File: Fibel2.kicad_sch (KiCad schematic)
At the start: 0 parts

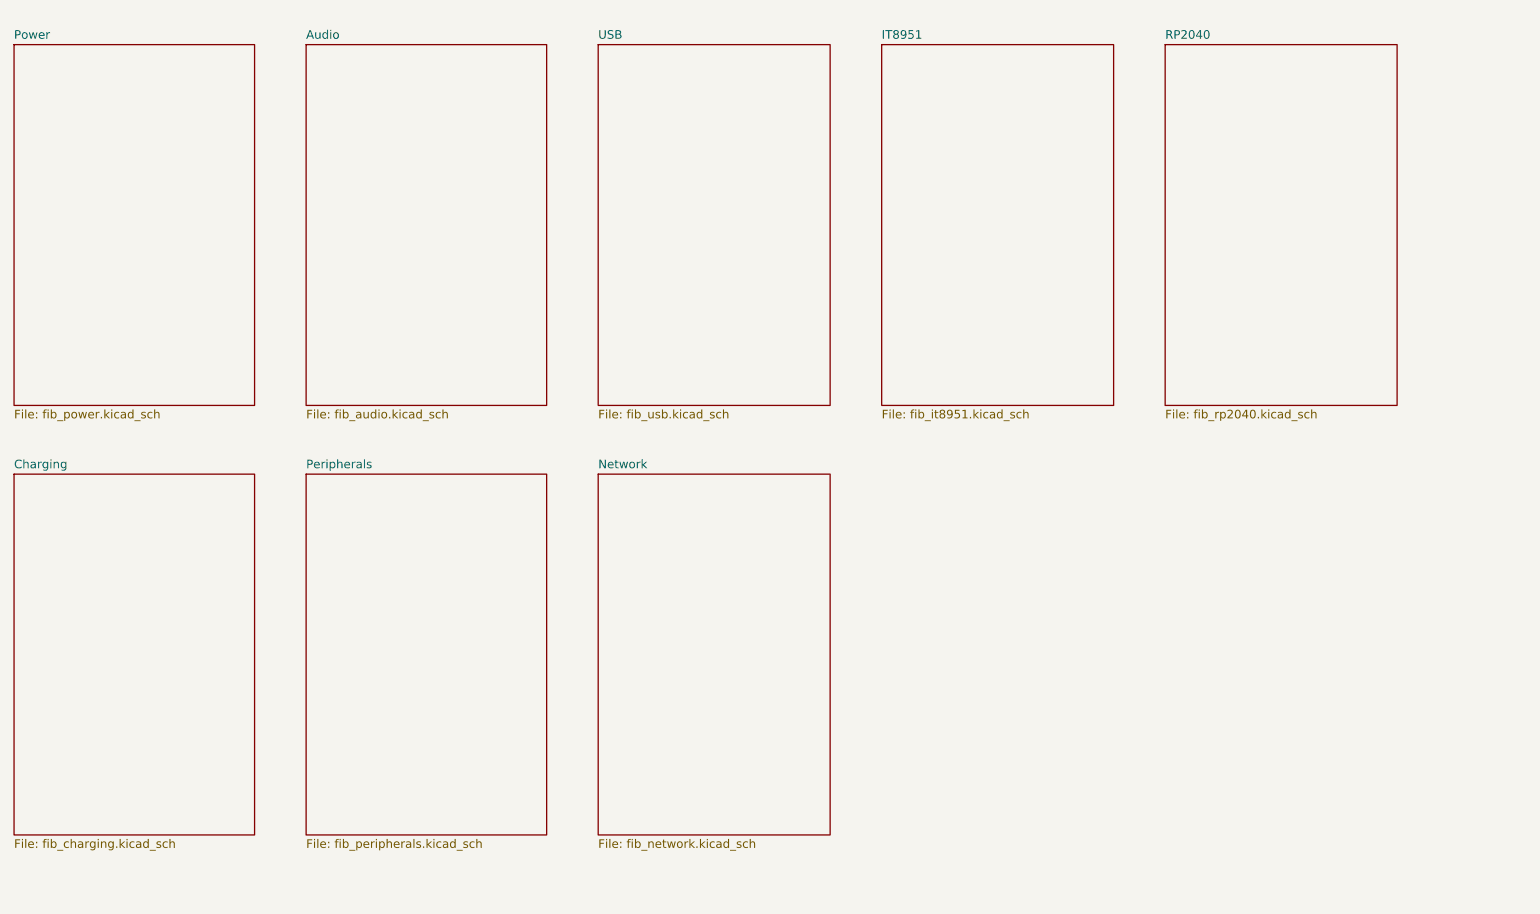
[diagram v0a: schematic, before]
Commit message: added several ICs, implementted schematics for charger, boost converter and LDOs
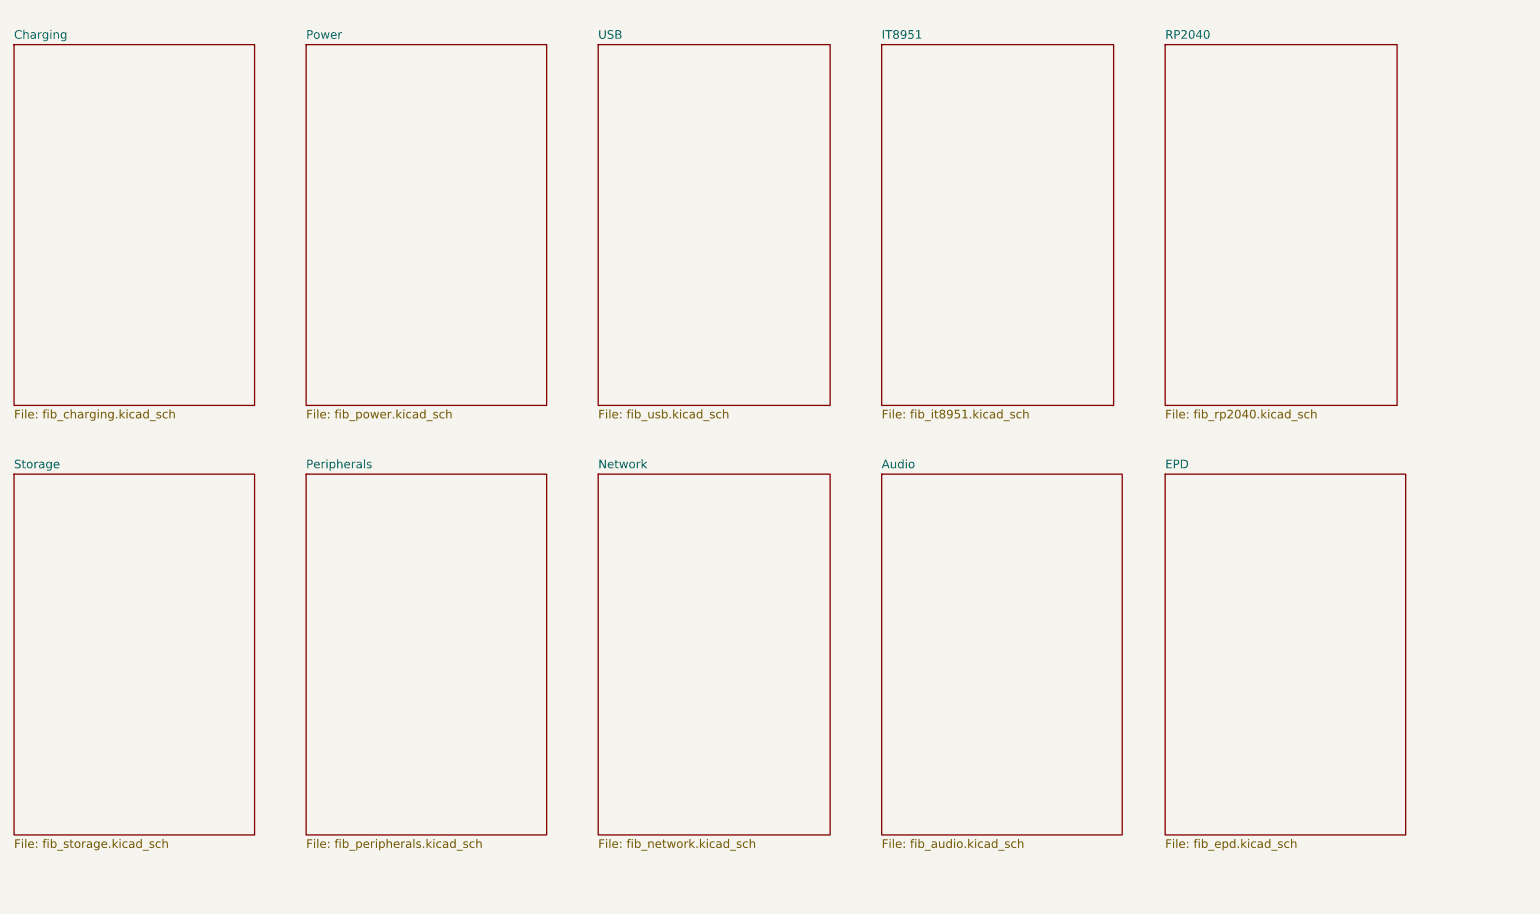
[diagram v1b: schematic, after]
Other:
- added sheet EPD (fib_epd.kicad_sch)
- added sheet Storage (fib_storage.kicad_sch)
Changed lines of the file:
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@@
 	(paper "A4")
 	(sheet
-		(at 69.85 21.59)
+		(at 154.94 85.09)
 		(size 35.56 53.34)
 		(fields_autoplaced yes)
@@
 		)
 		(property "Sheetname" "Audio"
-			(at 69.85 20.8784 0)
+			(at 154.94 84.3784 0)
 			(effects
 				(font
@@
 		)
 		(property "Sheetfile" "fib_audio.kicad_sch"
-			(at 69.85 75.5146 0)
+			(at 154.94 139.0146 0)
 			(effects
 				(font
@@
 	)
 	(sheet
-		(at 26.67 85.09)
+		(at 26.67 21.59)
 		(size 35.56 53.34)
 		(fields_autoplaced yes)
@@
 		)
 		(property "Sheetname" "Charging"
-			(at 26.67 84.3784 0)
+			(at 26.67 20.8784 0)
 			(effects
 				(font
@@
 		)
 		(property "Sheetfile" "fib_charging.kicad_sch"
-			(at 26.67 139.0146 0)
+			(at 26.67 75.5146 0)
 			(effects
 				(font
@@
 	)
 	(sheet
-		(at 26.67 21.59)
+		(at 196.85 85.09)
+		(size 35.56 53.34)
+		(fields_autoplaced yes)
+		(stroke
+			(width 0.1524)
+			(type solid)
+		)
+		(fill
+			(color 0 0 0 0.0000)
+		)
+		(property "Sheetname" "EPD"
+			(at 196.85 84.3784 0)
+			(effects
+				(font
+					(size 1.27 1.27)
+				)
+				(justify left bottom)
+			)
+		)
+		(property "Sheetfile" "fib_epd.kicad_sch"
+			(at 196.85 139.0146 0)
+			(effects
+				(font
+					(size 1.27 1.27)
+				)
+				(justify left top)
+			)
+		)
+		(instances
+			(project "Fibel2"
+				(path "/862c21e2-7ec9-4f80-a33c-aad02ea9423e"
+					(page "11")
+				)
+			)
+		)
+	)
+	(sheet
+		(at 26.67 85.09)
+		(size 35.56 53.34)
+		(fields_autoplaced yes)
+		(stroke
+			(width 0.1524)
+			(type solid)
+		)
+		(fill
+			(color 0 0 0 0.0000)
+		)
+		(property "Sheetname" "Storage"
+			(at 26.67 84.3784 0)
+			(effects
+				(font
+					(size 1.27 1.27)
+				)
+				(justify left bottom)
+			)
+		)
+		(property "Sheetfile" "fib_storage.kicad_sch"
+			(at 26.67 139.0146 0)
+			(effects
+				(font
+					(size 1.27 1.27)
+				)
+				(justify left top)
+			)
+		)
+		(instances
+			(project "Fibel2"
+				(path "/862c21e2-7ec9-4f80-a33c-aad02ea9423e"
+					(page "10")
+				)
+			)
+		)
+	)
+	(sheet
+		(at 69.85 21.59)
 		(size 35.56 53.34)
 		(fields_autoplaced yes)
@@
 		)
 		(property "Sheetname" "Power"
-			(at 26.67 20.8784 0)
+			(at 69.85 20.8784 0)
 			(effects
 				(font
@@
 		)
 		(property "Sheetfile" "fib_power.kicad_sch"
-			(at 26.67 75.5146 0)
-			(effects
-				(font
+			(at 69.85 75.5146 0)
+			(effects
+				(font

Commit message: added symbol&footprint for orin/sodimm, added a bunch of specs and docs, partially implemented audio, full steam ahead
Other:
- added sheet Orin_1 (fib_orin_1.kicad_sch)
- added sheet Orin_2 (fib_orin_2.kicad_sch)
- added sheet Orin_3 (fib_orin_3.kicad_sch)
- added sheet Orin_4 (fib_orin_4.kicad_sch)
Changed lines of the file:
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@@
 	(paper "A4")
 	(sheet
-		(at 154.94 85.09)
-		(size 35.56 53.34)
+		(at 154.94 63.5)
+		(size 35.56 38.1)
 		(fields_autoplaced yes)
 		(stroke
@@
 		)
 		(property "Sheetname" "Audio"
-			(at 154.94 84.3784 0)
+			(at 154.94 62.7884 0)
 			(effects
 				(font
@@
 		)
 		(property "Sheetfile" "fib_audio.kicad_sch"
-			(at 154.94 139.0146 0)
+			(at 154.94 101.5496 0)
 			(effects
 				(font
@@
 	)
 	(sheet
-		(at 26.67 21.59)
-		(size 35.56 53.34)
+		(at 26.67 20.32)
+		(size 35.56 38.1)
 		(fields_autoplaced yes)
 		(stroke
@@
 		)
 		(property "Sheetname" "Charging"
-			(at 26.67 20.8784 0)
+			(at 26.67 19.6084 0)
 			(effects
 				(font
@@
 		)
 		(property "Sheetfile" "fib_charging.kicad_sch"
-			(at 26.67 75.5146 0)
+			(at 26.67 58.3696 0)
 			(effects
 				(font
@@
 	)
 	(sheet
-		(at 196.85 21.59)
-		(size 34.29 53.34)
+		(at 196.85 20.32)
+		(size 34.29 38.1)
 		(fields_autoplaced yes)
 		(stroke
@@
 		)
 		(property "Sheetname" "RP2040"
-			(at 196.85 20.8784 0)
+			(at 196.85 19.05 0)
 			(effects
 				(font
@@
 		)
 		(property "Sheetfile" "fib_rp2040.kicad_sch"
-			(at 196.85 75.5146 0)
+			(at 196.85 58.3696 0)
 			(effects
 				(font
@@
 	)
 	(sheet
-		(at 196.85 85.09)
-		(size 35.56 53.34)
+		(at 113.03 106.68)
+		(size 35.56 38.1)
+		(fields_autoplaced yes)
+		(stroke
+			(width 0.1524)
+			(type solid)
+		)
+		(fill
+			(color 0 0 0 0.0000)
+		)
+		(property "Sheetname" "Orin_3"
+			(at 113.03 105.9684 0)
+			(effects
+				(font
+					(size 1.27 1.27)
+				)
+				(justify left bottom)
+			)
+		)
+		(property "Sheetfile" "fib_orin_3.kicad_sch"
+			(at 113.03 144.7296 0)
+			(effects
+				(font
+					(size 1.27 1.27)
+				)
+				(justify left top)
+			)
+		)
+		(instances
+			(project "Fibel2"
+				(path "/862c21e2-7ec9-4f80-a33c-aad02ea9423e"
+					(page "14")
+				)
+			)
+		)
+	)
+	(sheet
+		(at 196.85 63.5)
+		(size 35.56 38.1)
 		(fields_autoplaced yes)
 		(stroke
@@
 		)
 		(property "Sheetname" "EPD"
-			(at 196.85 84.3784 0)
+			(at 196.85 62.7884 0)
 			(effects
 				(font
@@
 		)
 		(property "Sheetfile" "fib_epd.kicad_sch"
-			(at 196.85 139.0146 0)
+			(at 196.85 101.5496 0)
 			(effects
 				(font
@@
 	)
 	(sheet
-		(at 26.67 85.09)
-		(size 35.56 53.34)
+		(at 69.85 106.68)
+		(size 35.56 38.1)
+		(fields_autoplaced yes)
+		(stroke
+			(width 0.1524)
+			(type solid)
+		)
+		(fill
+			(color 0 0 0 0.0000)
+		)
+		(property "Sheetname" "Orin_2"
+			(at 69.85 105.9684 0)
+			(effects
+				(font
+					(size 1.27 1.27)
+				)
+				(justify left bottom)
+			)
+		)
+		(property "Sheetfile" "fib_orin_2.kicad_sch"
+			(at 69.85 144.7296 0)
+			(effects
+				(font
+					(size 1.27 1.27)
+				)
+				(justify left top)
+			)
+		)
+		(instances
+			(project "Fibel2"
+				(path "/862c21e2-7ec9-4f80-a33c-aad02ea9423e"
+					(page "13")
+				)
+			)
+		)
+	)
+	(sheet
+		(at 26.67 63.5)
+		(size 35.56 38.1)
 		(fields_autoplaced yes)
 		(stroke
@@
 		)
 		(property "Sheetname" "Storage"
-			(at 26.67 84.3784 0)
+			(at 26.67 62.7884 0)
 			(effects
 				(font
@@
 		)
 		(property "Sheetfile" "fib_storage.kicad_sch"
-			(at 26.67 139.0146 0)
+			(at 26.67 101.5496 0)
 			(effects
 				(font
@@
 	)
 	(sheet
-		(at 69.85 21.59)
-		(size 35.56 53.34)
+		(at 69.85 20.32)
+		(size 35.56 38.1)
 		(fields_autoplaced yes)
 		(stroke
@@
 		)
 		(property "Sheetname" "Power"
-			(at 69.85 20.8784 0)
+			(at 69.85 19.6084 0)
 			(effects
 				(font
@@
 		)
 		(property "Sheetfile" "fib_power.kicad_sch"
-			(at 69.85 75.5146 0)
+			(at 69.85 58.3696 0)
 			(effects
 				(font
@@
 	)
 	(sheet
-		(at 113.03 21.59)
-		(size 34.29 53.34)
+		(at 113.03 20.32)
+		(size 34.29 38.1)
 		(fields_autoplaced yes)
 		(stroke
@@
 		)
 		(property "Sheetname" "USB"
-			(at 113.03 20.8784 0)
+			(at 113.03 19.6084 0)
 			(effects
 				(font
@@
 		)
 		(property "Sheetfile" "fib_usb.kicad_sch"
-			(at 113.03 75.5146 0)
+			(at 113.03 58.3696 0)
 			(effects
 				(font
@@
 	)
 	(sheet
-		(at 69.85 85.09)
-		(size 35.56 53.34)
+		(at 69.85 63.5)
+		(size 35.56 38.1)
 		(fields_autoplaced yes)
 		(stroke
@@
 		)
 		(property "Sheetname" "Peripherals"
-			(at 69.85 84.3784 0)
+			(at 69.85 62.7884 0)
 			(effects
 				(font
@@
 		)
 		(property "Sheetfile" "fib_peripherals.kicad_sch"
-			(at 69.85 139.0146 0)
+			(at 69.85 101.5496 0)
 			(effects
 				(font
@@
 	)
 	(sheet
-		(at 113.03 85.09)
-		(size 34.29 53.34)
+		(at 113.03 63.5)
+		(size 34.29 38.1)
 		(fields_autoplaced yes)
 		(stroke
@@
 		)
 		(property "Sheetname" "Network"
-			(at 113.03 84.3784 0)
+			(at 113.03 62.7884 0)
 			(effects
 				(font
@@
 		)
 		(property "Sheetfile" "fib_network.kicad_sch"
-			(at 113.03 139.0146 0)
+			(at 113.03 101.5496 0)
 			(effects
 				(font
@@
 	)
 	(sheet
-		(at 154.94 21.59)
-		(size 34.29 53.34)
+		(at 26.67 106.68)
+		(size 35.56 38.1)
+		(fields_autoplaced yes)
+		(stroke
+			(width 0.1524)
+			(type solid)
+		)
+		(fill
+			(color 0 0 0 0.0000)
+		)
+		(property "Sheetname" "Orin_1"
+			(at 26.67 105.9684 0)
+			(effects
+				(font
+					(size 1.27 1.27)
+				)
+				(justify left bottom)
+			)
+		)
+		(property "Sheetfile" "fib_orin_1.kicad_sch"
+			(at 26.67 144.7296 0)
+			(effects
+				(font
+					(size 1.27 1.27)
+				)
+				(justify left top)
+			)
+		)
+		(instances
+			(project "Fibel2"
+				(path "/862c21e2-7ec9-4f80-a33c-aad02ea9423e"
+					(page "12")
+				)
+			)
+		)
+	)
+	(sheet
+		(at 154.94 106.68)
+		(size 35.56 38.1)
+		(fields_autoplaced yes)
+		(stroke
+			(width 0.1524)
+			(type solid)
+		)
+		(fill
+			(color 0 0 0 0.0000)
+		)
+		(property "Sheetname" "Orin_4"
+			(at 154.94 105.9684 0)
+			(effects
+				(font
+					(size 1.27 1.27)
+				)
+				(justify left bottom)
+			)
+		)
+		(property "Sheetfile" "fib_orin_4.kicad_sch"
+			(at 154.94 144.7296 0)
+			(effects
+				(font
+					(size 1.27 1.27)
+				)
+				(justify left top)
+			)
+		)
+		(instances
+			(project "Fibel2"
+				(path "/862c21e2-7ec9-4f80-a33c-aad02ea9423e"
+					(page "15")
+				)
+			)
+		)
+	)
+	(sheet
+		(at 154.94 20.32)
+		(size 34.29 38.1)
 		(fields_autoplaced yes)
 		(stroke
@@
 		)
 		(property "Sheetname" "IT8951"
-			(at 154.94 20.8784 0)
+			(at 154.94 19.6084 0)
 			(effects
 				(font
@@
 		)
 		(property "Sheetfile" "fib_it8951.kicad_sch"
-			(at 154.94 75.5146 0)
-			(effects
-				(font
+			(at 154.94 58.3696 0)
+			(effects
+				(font

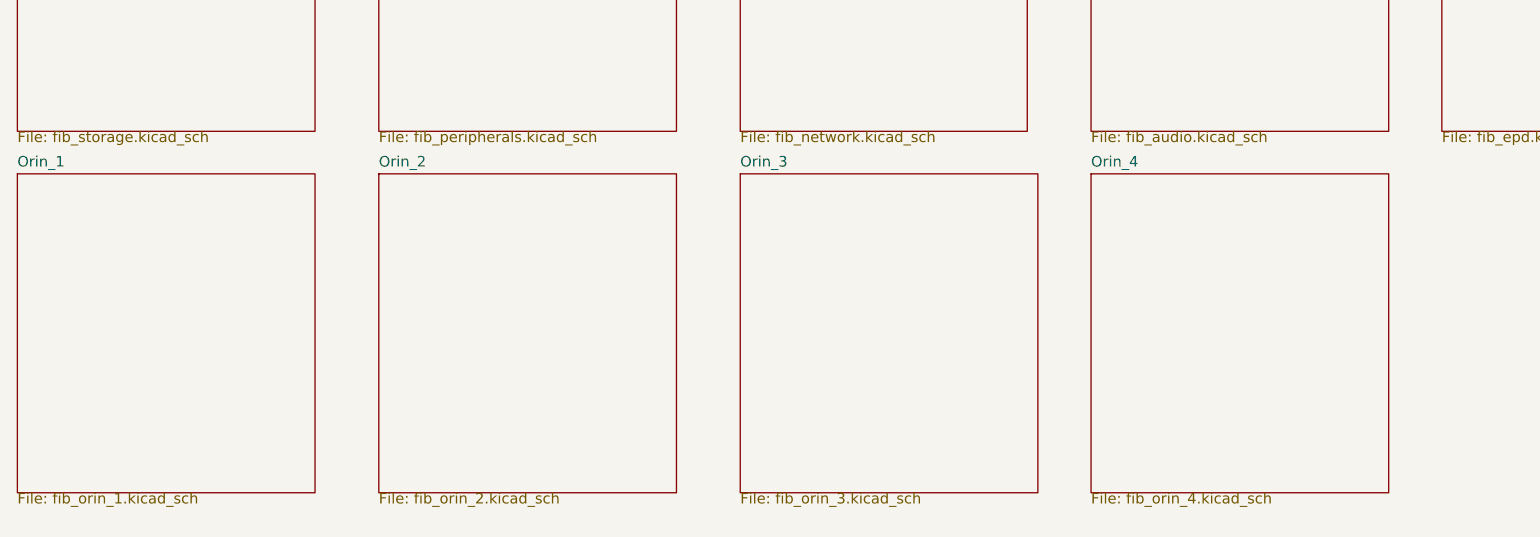
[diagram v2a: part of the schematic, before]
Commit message: added nets for 40 pin headers (epd & rpi header) connected some of the nets i'm reeusing
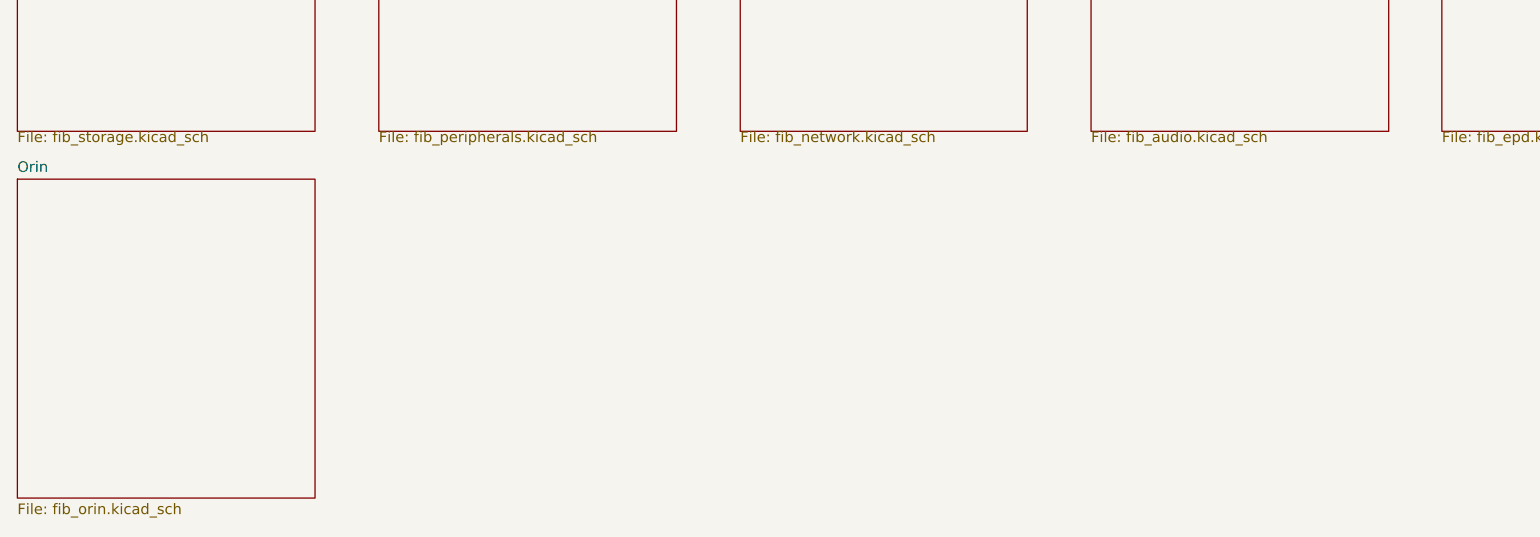
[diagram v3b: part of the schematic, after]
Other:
- removed sheet Orin_1
- removed sheet Orin_2
- removed sheet Orin_3
- removed sheet Orin_4
- added sheet Orin (fib_orin.kicad_sch)
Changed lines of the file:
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@@
 			(project "Fibel2"
 				(path "/862c21e2-7ec9-4f80-a33c-aad02ea9423e"
-					(page "7")
+					(page "6")
 				)
 			)
@@
 			(project "Fibel2"
 				(path "/862c21e2-7ec9-4f80-a33c-aad02ea9423e"
-					(page "3")
+					(page "2")
 				)
 			)
@@
 			(project "Fibel2"
 				(path "/862c21e2-7ec9-4f80-a33c-aad02ea9423e"
-					(page "6")
-				)
-			)
-		)
-	)
-	(sheet
-		(at 113.03 106.68)
-		(size 35.56 38.1)
-		(fields_autoplaced yes)
-		(stroke
-			(width 0.1524)
-			(type solid)
-		)
-		(fill
-			(color 0 0 0 0.0000)
-		)
-		(property "Sheetname" "Orin_3"
-			(at 113.03 105.9684 0)
-			(effects
-				(font
-					(size 1.27 1.27)
-				)
-				(justify left bottom)
-			)
-		)
-		(property "Sheetfile" "fib_orin_3.kicad_sch"
-			(at 113.03 144.7296 0)
-			(effects
-				(font
-					(size 1.27 1.27)
-				)
-				(justify left top)
-			)
-		)
-		(instances
-			(project "Fibel2"
-				(path "/862c21e2-7ec9-4f80-a33c-aad02ea9423e"
-					(page "14")
+					(page "5")
+				)
+			)
+		)
+	)
+	(sheet
+		(at 26.67 107.315)
+		(size 35.56 38.1)
+		(fields_autoplaced yes)
+		(stroke
+			(width 0.1524)
+			(type solid)
+		)
+		(fill
+			(color 0 0 0 0.0000)
+		)
+		(property "Sheetname" "Orin"
+			(at 26.67 106.6034 0)
+			(effects
+				(font
+					(size 1.27 1.27)
+				)
+				(justify left bottom)
+			)
+		)
+		(property "Sheetfile" "fib_orin.kicad_sch"
+			(at 26.67 145.9996 0)
+			(effects
+				(font
+					(size 1.27 1.27)
+				)
+				(justify left top)
+			)
+		)
+		(instances
+			(project "Fibel2"
+				(path "/862c21e2-7ec9-4f80-a33c-aad02ea9423e"
+					(page "11")
 				)
 			)
@@
 			(project "Fibel2"
 				(path "/862c21e2-7ec9-4f80-a33c-aad02ea9423e"
-					(page "11")
-				)
-			)
-		)
-	)
-	(sheet
-		(at 69.85 106.68)
-		(size 35.56 38.1)
-		(fields_autoplaced yes)
-		(stroke
-			(width 0.1524)
-			(type solid)
-		)
-		(fill
-			(color 0 0 0 0.0000)
-		)
-		(property "Sheetname" "Orin_2"
-			(at 69.85 105.9684 0)
-			(effects
-				(font
-					(size 1.27 1.27)
-				)
-				(justify left bottom)
-			)
-		)
-		(property "Sheetfile" "fib_orin_2.kicad_sch"
-			(at 69.85 144.7296 0)
-			(effects
-				(font
-					(size 1.27 1.27)
-				)
-				(justify left top)
-			)
-		)
-		(instances
-			(project "Fibel2"
-				(path "/862c21e2-7ec9-4f80-a33c-aad02ea9423e"
-					(page "13")
+					(page "10")
 				)
 			)
@@
 			(project "Fibel2"
 				(path "/862c21e2-7ec9-4f80-a33c-aad02ea9423e"
-					(page "10")
+					(page "9")
 				)
 			)
@@
 			(project "Fibel2"
 				(path "/862c21e2-7ec9-4f80-a33c-aad02ea9423e"
-					(page "2")
+					(page "1")
 				)
 			)
@@
 			(project "Fibel2"
 				(path "/862c21e2-7ec9-4f80-a33c-aad02ea9423e"
-					(page "4")
+					(page "3")
 				)
 			)
@@
 			(project "Fibel2"
 				(path "/862c21e2-7ec9-4f80-a33c-aad02ea9423e"
-					(page "8")
+					(page "7")
 				)
 			)
@@
 			(project "Fibel2"
 				(path "/862c21e2-7ec9-4f80-a33c-aad02ea9423e"
-					(page "9")
-				)
-			)
-		)
-	)
-	(sheet
-		(at 26.67 106.68)
-		(size 35.56 38.1)
-		(fields_autoplaced yes)
-		(stroke
-			(width 0.1524)
-			(type solid)
-		)
-		(fill
-			(color 0 0 0 0.0000)
-		)
-		(property "Sheetname" "Orin_1"
-			(at 26.67 105.9684 0)
-			(effects
-				(font
-					(size 1.27 1.27)
-				)
-				(justify left bottom)
-			)
-		)
-		(property "Sheetfile" "fib_orin_1.kicad_sch"
-			(at 26.67 144.7296 0)
-			(effects
-				(font
-					(size 1.27 1.27)
-				)
-				(justify left top)
-			)
-		)
-		(instances
-			(project "Fibel2"
-				(path "/862c21e2-7ec9-4f80-a33c-aad02ea9423e"
-					(page "12")
-				)
-			)
-		)
-	)
-	(sheet
-		(at 154.94 106.68)
-		(size 35.56 38.1)
-		(fields_autoplaced yes)
-		(stroke
-			(width 0.1524)
-			(type solid)
-		)
-		(fill
-			(color 0 0 0 0.0000)
-		)
-		(property "Sheetname" "Orin_4"
-			(at 154.94 105.9684 0)
-			(effects
-				(font
-					(size 1.27 1.27)
-				)
-				(justify left bottom)
-			)
-		)
-		(property "Sheetfile" "fib_orin_4.kicad_sch"
-			(at 154.94 144.7296 0)
-			(effects
-				(font
-					(size 1.27 1.27)
-				)
-				(justify left top)
-			)
-		)
-		(instances
-			(project "Fibel2"
-				(path "/862c21e2-7ec9-4f80-a33c-aad02ea9423e"
-					(page "15")
+					(page "8")
 				)
 			)
@@
 			(project "Fibel2"
 				(path "/862c21e2-7ec9-4f80-a33c-aad02ea9423e"
-					(page "5")
+					(page "4")
 				)
 			)
@@
 	(sheet_instances
 		(path "/"
-			(page "1")
-		)
-	)
+			(page "0")
+		)
+	)
